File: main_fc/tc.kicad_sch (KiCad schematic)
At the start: 11 parts, among them U2 AD8495

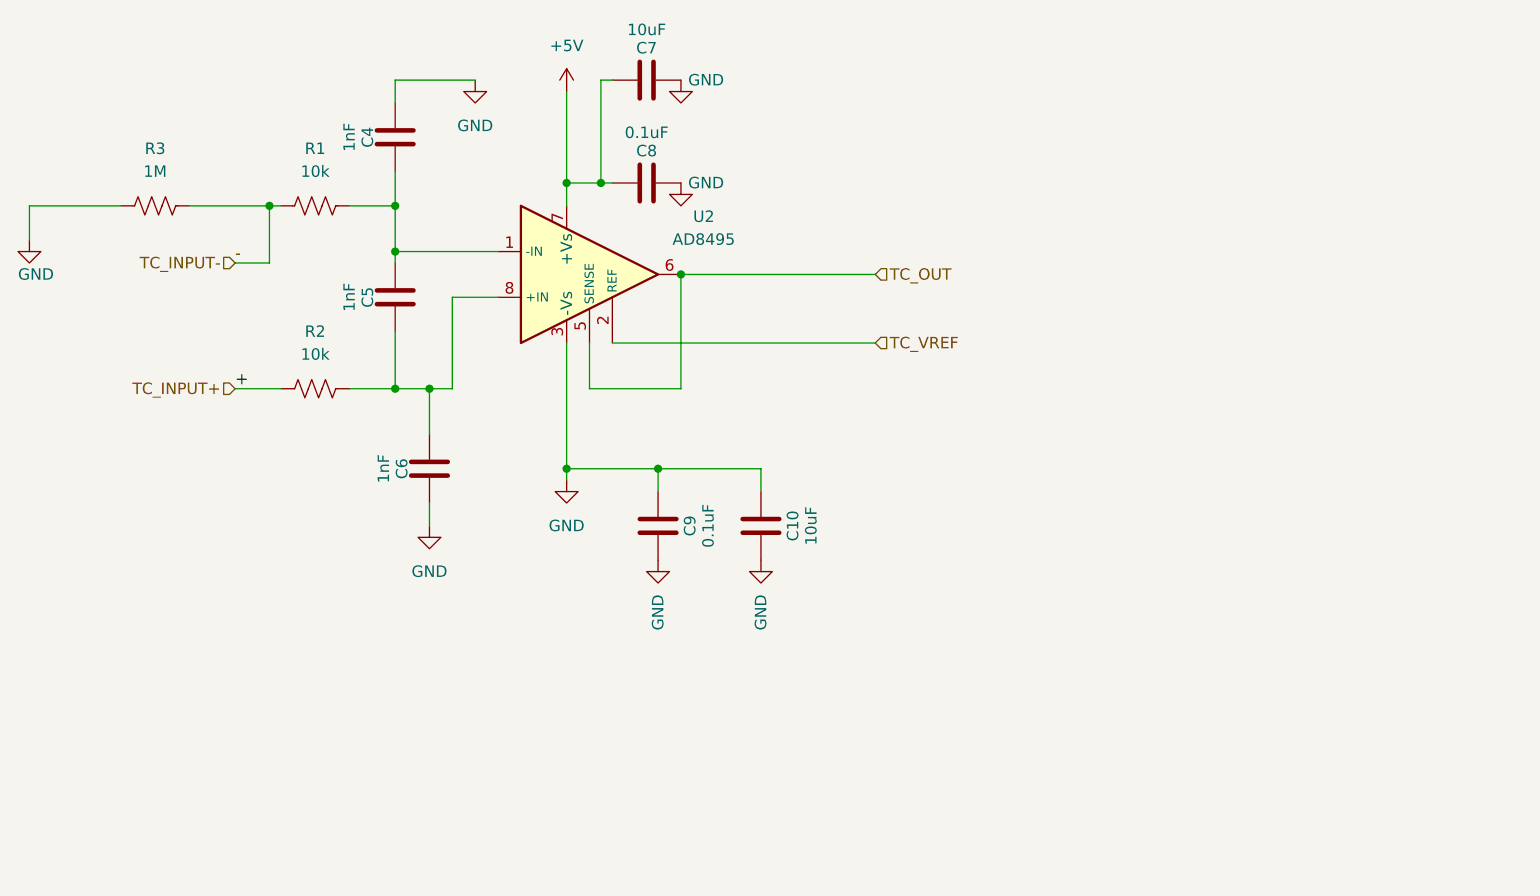
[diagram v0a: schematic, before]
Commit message: main flight computer annotations and passive footprints
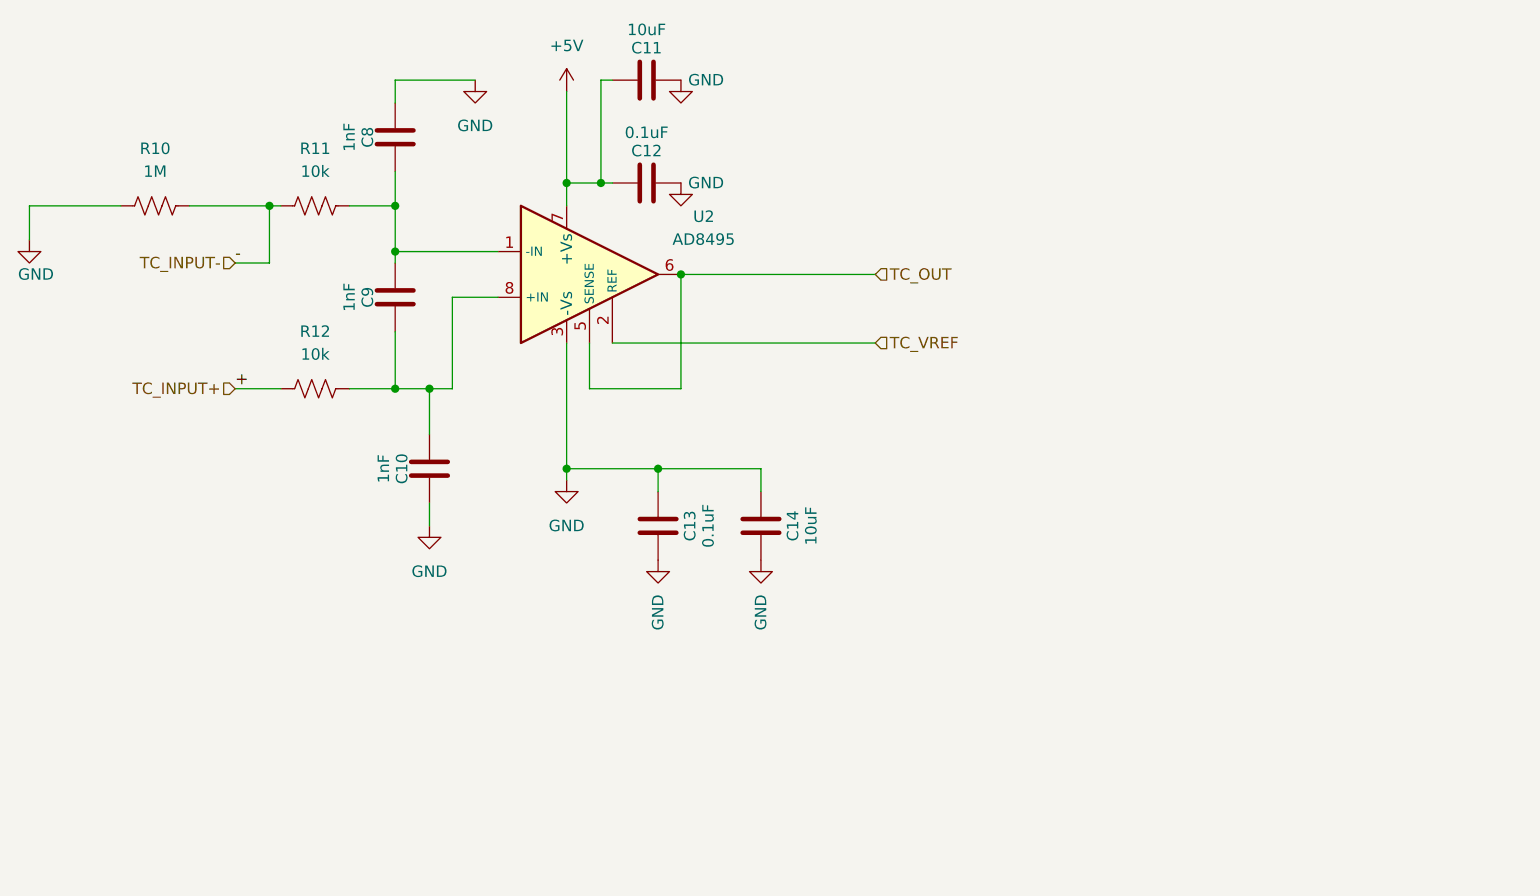
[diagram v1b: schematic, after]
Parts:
- R10: renamed from R3; footprint Resistor_SMD:R_0201_0603Metric -> Resistor_SMD:R_0603_1608Metric
- R11: renamed from R1; footprint Resistor_SMD:R_0201_0603Metric -> Resistor_SMD:R_0603_1608Metric
- R12: renamed from R2; footprint Resistor_SMD:R_0201_0603Metric -> Resistor_SMD:R_0603_1608Metric
- renumbered C6 to C10, C7 to C11, C8 to C12, C9 to C13, C10 to C14, C4 to C8, C5 to C9

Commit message: updated library
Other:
- moved on the sheet: C10, C11, C12, C13, C14, C8, C9, R10, R11, R12, U2

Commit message: updated TC routing
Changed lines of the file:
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@@
-		)
-	)
-	(label "+"
-		(at 105.41 93.98 0)
-		(effects
-			(font
-				(size 1.27 1.27)
-			)
-			(justify left bottom)
-		)
-	)
-	(label "-"
-		(at 105.41 80.01 0)
-		(effects
-			(font
-				(size 1.27 1.27)
-			)
-			(justify left bottom)
 		)
 	)

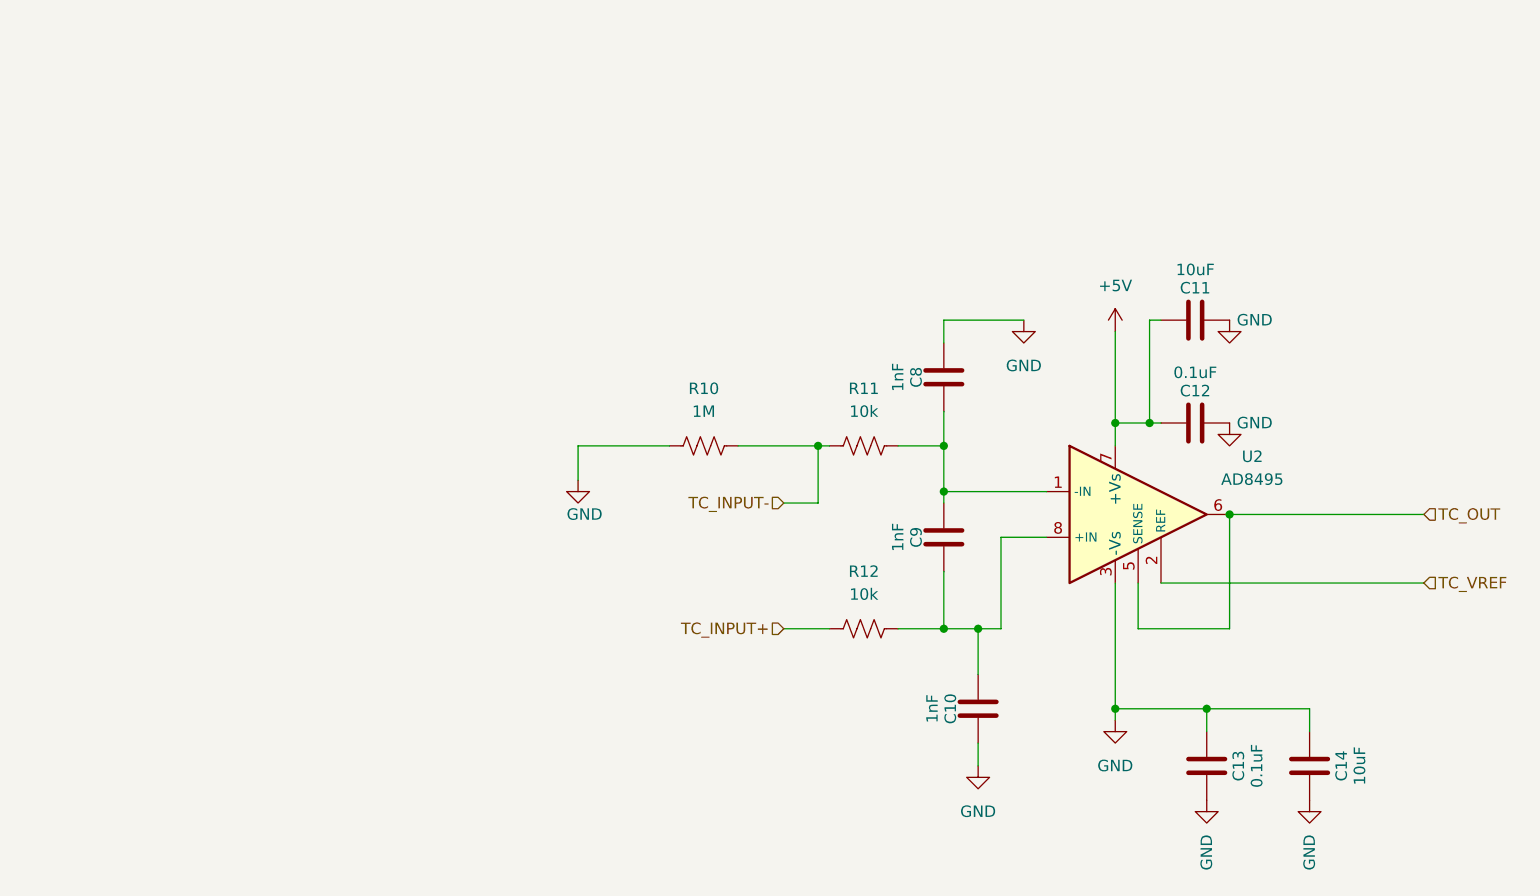
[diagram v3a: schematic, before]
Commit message: added new stm symbol/footprint
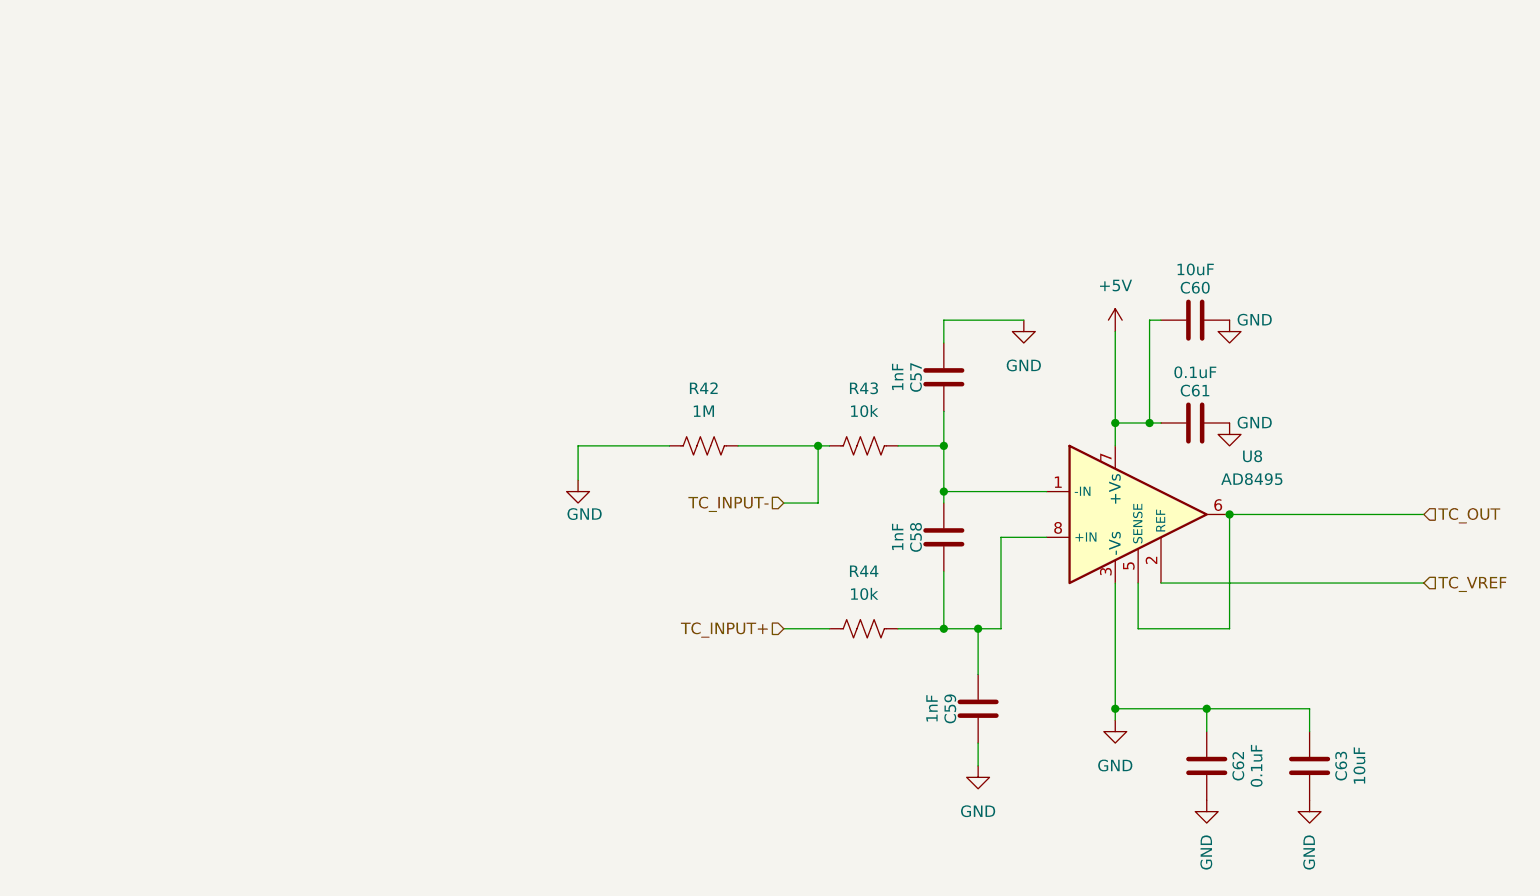
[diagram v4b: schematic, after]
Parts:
- renumbered C8 to C57, C9 to C58, C10 to C59, C11 to C60, C12 to C61, C13 to C62, C14 to C63, R10 to R42, R11 to R43, R12 to R44, U2 to U8
